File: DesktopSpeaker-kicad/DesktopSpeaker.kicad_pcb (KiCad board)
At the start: 4 copper layers, 136.9 x 127.8 mm, 351 parts, among them J1 USB_C_Receptacle_USB2.0_16P, J10 B2P-VH, J11 B2P-VH, J2 HEAD_OUT, J3 AUX_IN, J4 I2C service, J5 1S_PACK_3PIN, J6 SWD, J7 SWD_TC2030, J8 BM83_PROG, J9 B2P-VH, Q100 2N7002, Q101 2N7002, Q102 2N7002, Q103 CSD17579Q3A, Q104 2N7002, SW100 WAKE_QON, SW101 BAT_DISCONNECT, SW102 EC11E, U1 BM83SM1-00TA, U10 TPA6132A2RTER, U11 TPS25730DREFR, U12 TPS7A0230PDBVR, U13 TS5A3167DBVR, U14 TPS63802DLAR, U15 TPS63802DLAR, U16 TS5A3167DBVR, U17 TS5A3167DBVR, U19 TPS7B8450QWDRBRQ1, U2 PCM2902CDBR, U20 TPS2116DRLR, U21 TPS3839G33DBZR, U22 TPS7A2033PDBVR, U23 TPS22917DBVR, U24 PCM1862DBTR, U25 TPS61088RHLR, U3 STM32G071RBT6, U4 BQ25792RQMR, U5 MAX17048G+T10, U6 TAS5825MRHBR, U7 TAS5825MRHBR, U8 TS5A23157DGSR, U9 TS5A23157DGSR, Y170 12MHz, Y200 24.576MHz

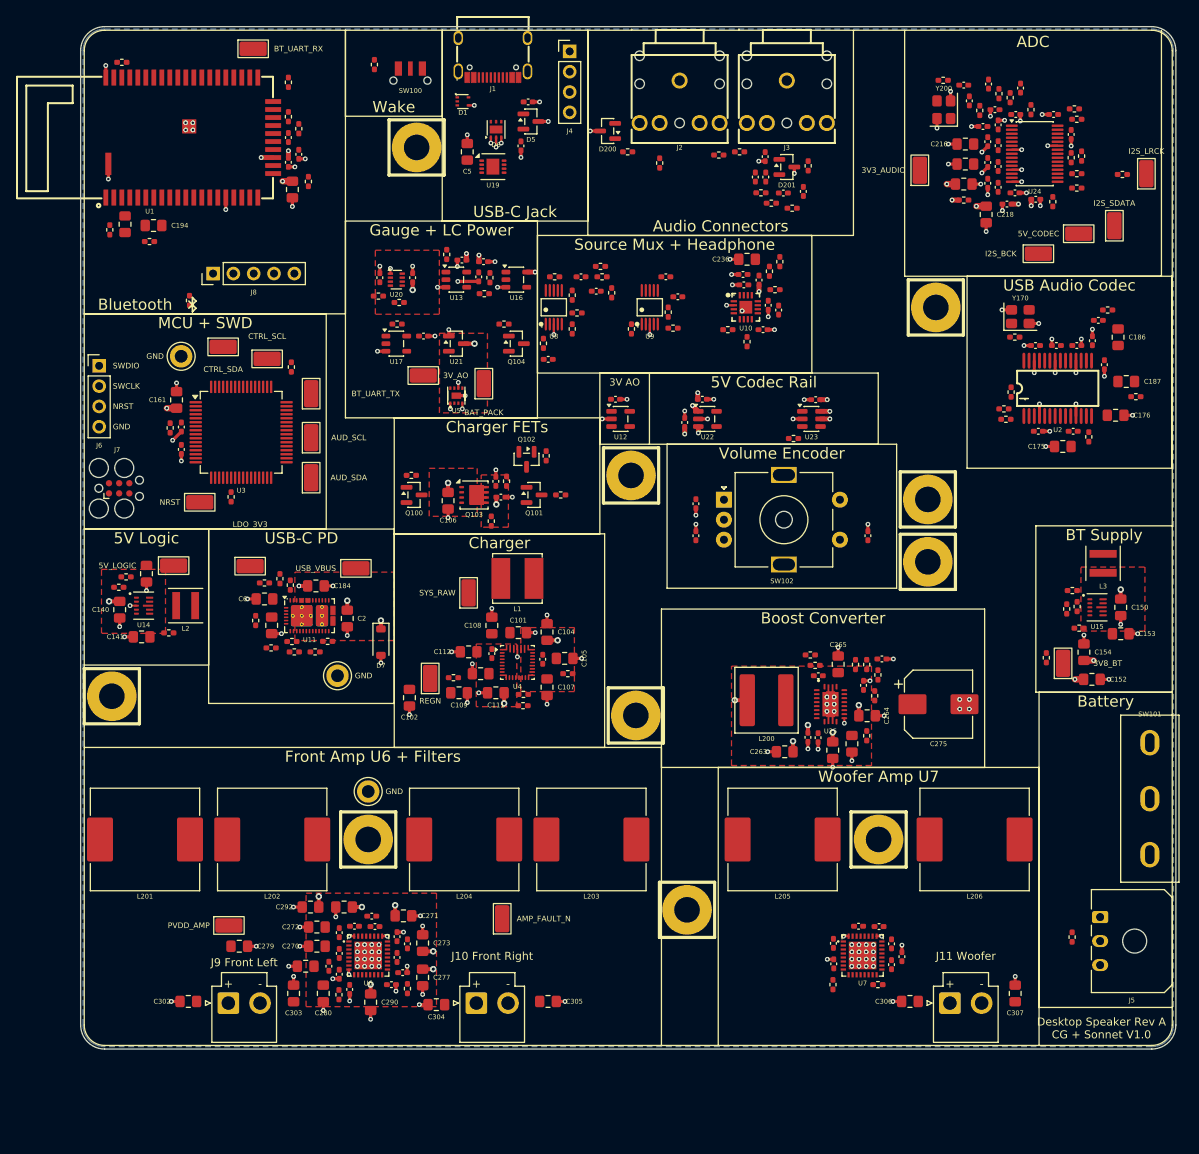
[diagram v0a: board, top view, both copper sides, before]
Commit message: Routing R6a-R6m adopted into project board; ERC cleanup, MCU pin swaps, C241 2.2uF, SW100 footprint fix, reviews and helpers
Co-Authored-By: Claude Sonnet 5.5 <noreply@anthropic.com>
Claude-Session: https://claude.ai/code/session_016fe4xPJbEE2SjGafuyNLjb
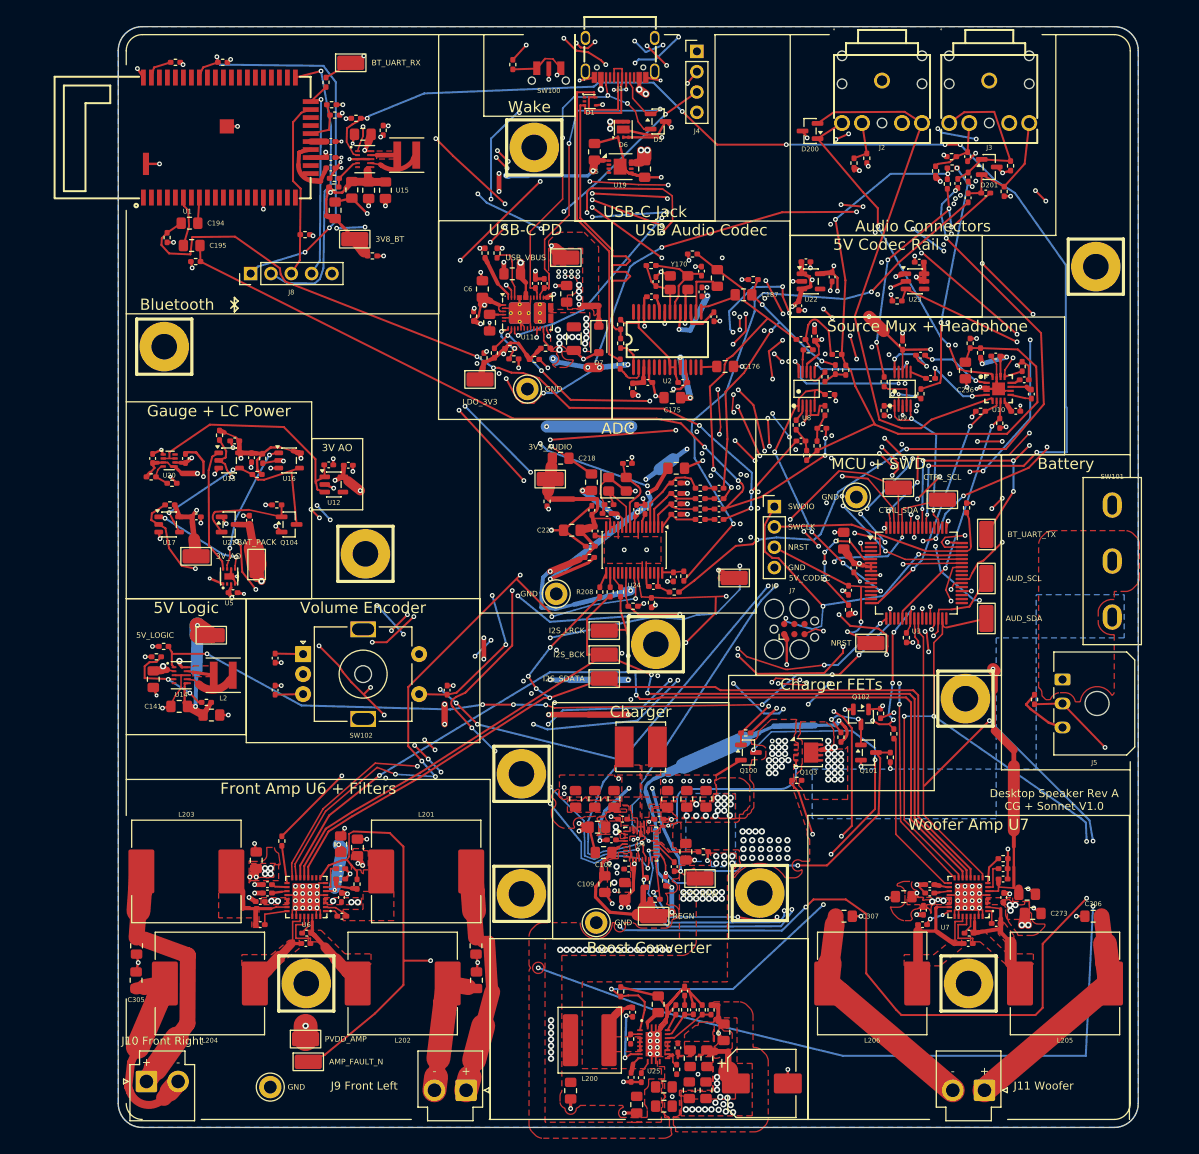
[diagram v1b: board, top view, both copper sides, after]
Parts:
- added C311: 100nF, DesktopSpeaker:C_0402_1005Metric_Pad0.74x0.62mm_HandSolder, F.Cu at (153.8, 119.1)
- added C312: 100nF, DesktopSpeaker:C_0402_1005Metric_Pad0.74x0.62mm_HandSolder, F.Cu at (149.3, 119.1)
- added C313: 100nF, DesktopSpeaker:C_0402_1005Metric_Pad0.74x0.62mm_HandSolder, F.Cu at (150.1, 125.3)
- added C314: 100nF, DesktopSpeaker:C_0402_1005Metric_Pad0.74x0.62mm_HandSolder, F.Cu at (156.2, 147.7)
- added C315: 47uF 25V, DesktopSpeaker:PD_C_1206, F.Cu at (143.2, 59.0)
- added C316: 1uF X7R 50V, DesktopSpeaker:C_0805_2012Metric_Pad1.18x1.45mm_HandSolder, F.Cu at (152.1, 37.8)
- added H8: M3 PTH GND, DesktopSpeaker:MountingHole_3.2mm_M3_PTH_GND, F.Cu at (117.2, 85.9)
- added TP26: GND, DesktopSpeaker:TestPoint_Keystone_5010-5014_Multipurpose, F.Cu at (141.0, 90.9)
- added TP27: GND, DesktopSpeaker:TestPoint_Keystone_5010-5014_Multipurpose, F.Cu at (146.0, 132.0)
- C241: value 1uF -> 2.2uF
- moved C150 111.7 mm to (116.8, 33.5), turned to 180 degrees
- moved C152 109.1 mm to (117.5, 40.5), turned to -90 degrees
- moved C154 108.7 mm to (113.4, 43.0)
- moved R150 108.3 mm to (113.2, 40.0), turned to 0 degrees
- moved R153 108.0 mm to (116.0, 31.5), turned to 180 degrees
- moved C153 107.3 mm to (119.7, 40.5), turned to -90 degrees
- moved U15 107.3 mm to (117.1, 36.6)
- moved R151 107.2 mm to (113.3, 39.0), turned to 180 degrees
- moved R152 103.6 mm to (119.4, 33.0), turned to 90 degrees
- moved TP9 103.2 mm to (115.8, 46.6), turned to 0 degrees
- moved H3 102.6 mm to (166.4, 128.3)
- moved L3 100.9 mm to (122.3, 36.1), turned to 0 degrees
- moved R154 98.1 mm to (118.0, 48.7), turned to 0 degrees
- moved H7 97.2 mm to (138.2, 35.1)
- moved H9 96.6 mm to (92.0, 60.0)
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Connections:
- TP13 pad 1: /I2S_LRCK -> /I2S_SDATA
- TP14 pad 1: /I2S_SDATA -> /I2S_LRCK
- U3 pad 14: /HP_SEL_B -> unconnected-(U3-PC1-Pad14)
- U3 pad 15: /HP_EN -> unconnected-(U3-PC2-Pad15)
- U3 pad 18: unconnected-(U3-PA1-Pad18) -> /5V_LOGIC_EN
- U3 pad 19: /BT_UART_TX -> unconnected-(U3-PA2-Pad19)
- U3 pad 20: /BT_UART_RX -> unconnected-(U3-PA3-Pad20)
- U3 pad 37: /BT_FORCE_PWM -> unconnected-(U3-PA9-Pad37)
- U3 pad 47: unconnected-(U3-PA15-Pad47) -> /HP_EN
- U3 pad 51: unconnected-(U3-PD1-Pad51) -> /HP_SEL_B
- U3 pad 54: unconnected-(U3-PD4-Pad54) -> /BT_FORCE_PWM
- U3 pad 55: unconnected-(U3-PD5-Pad55) -> /BT_UART_TX
- U3 pad 56: unconnected-(U3-PD6-Pad56) -> /BT_UART_RX
- U3 pad 59: /5V_LOGIC_EN -> unconnected-(U3-PB5-Pad59)
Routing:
- net /3V3_AUDIO: track 5.72 -> 299.6 mm, vias 6 -> 20
- net /AUD_SDA: track 0.00 -> 277.9 mm, vias 0 -> 13
- net /AMP_FAULT_N: track 0.00 -> 231.7 mm, vias 0 -> 5
- net GND: track 159.0 -> 364.4 mm, vias 203 -> 267
- net /MCU/ENC_SW: track 0.00 -> 203.5 mm, vias 0 -> 17
- net /3V_AO: track 3.90 -> 200.8 mm, vias 4 -> 11
- net /BT_RST_N: track 0.00 -> 187.2 mm, vias 0 -> 8
- net /CTRL_SDA: track 0.00 -> 172.3 mm, vias 0 -> 16
- net /AUD_SCL: track 0.00 -> 158.4 mm, vias 0 -> 10
- net /BT_FORCE_PWM: track 0.00 -> 154.5 mm, vias 0 -> 8
- net /PDCTRL_SDA: track 0.00 -> 148.5 mm, vias 0 -> 16
- net /BT_UART_TX: track 0.00 -> 146.3 mm, vias 0 -> 18
- net /CTRL_SCL: track 0.00 -> 141.4 mm, vias 0 -> 12
- net /BT_UART_RX: track 0.00 -> 140.7 mm, vias 0 -> 8
- net /BT_PWR_EN: track 0.00 -> 140.4 mm, vias 0 -> 7
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- added copper zone on F.Cu, net /Battery_Charger/PACK_RAW
- added copper zone on F.Cu, net /Battery_Charger/PMID
- added copper zone on F.Cu, net /Battery_Charger/SW1
- added copper zone on F.Cu, net /Battery_Charger/SW2
- added copper zone on B.Cu, net /Fuel_Gauge_Power/BAT_PACK
- added copper zone on B.Cu, net /SYS_RAW
- added copper zone on F.Cu, net GND
- added copper zone on In2.Cu, net GND
- added copper zone on F.Cu, net Net-(U14-L1)
- added copper zone on F.Cu, net Net-(U15-L1)
- added copper zone on F.Cu, net Net-(U25-SW)
- added copper zone on F.Cu, net Net-(U6-OUT_A+)
- added copper zone on F.Cu, net Net-(U6-OUT_A-)
- added copper zone on F.Cu, net Net-(U6-OUT_B+)
- added copper zone on F.Cu, net Net-(U6-OUT_B-)
- added copper zone on F.Cu, net Net-(U7-OUT_A+)
- added copper zone on F.Cu, net Net-(U7-OUT_B+)
- removed copper zone on In2.Cu, net /3V3_AUDIO
- removed copper zone on In2.Cu, net /3V8_BT
- removed copper zone on In2.Cu, net /3V_AO
- removed copper zone on In2.Cu, net /5V_CODEC
- removed copper zone on In2.Cu, net /5V_LOGIC
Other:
- board size 136.9 x 127.8 mm -> 127.5 x 137.6 mm
- board text removed: "BT Supply"

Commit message: Y200 24.576 MHz crystal with 15 pF load caps, C275 3D model, schematic/PCB sourcing fields synced to BOM
Co-Authored-By: Claude Sonnet 5.5 <noreply@anthropic.com>
Claude-Session: https://claude.ai/code/session_016fe4xPJbEE2SjGafuyNLjb
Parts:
- C226, C227: value 22pF C0G -> 15pF C0G
